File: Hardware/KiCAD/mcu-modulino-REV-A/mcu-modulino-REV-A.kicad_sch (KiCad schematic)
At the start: 9 parts, among them SW1 SW_Push, SW2 SW_Push, U8 ESP32-WROVER-E

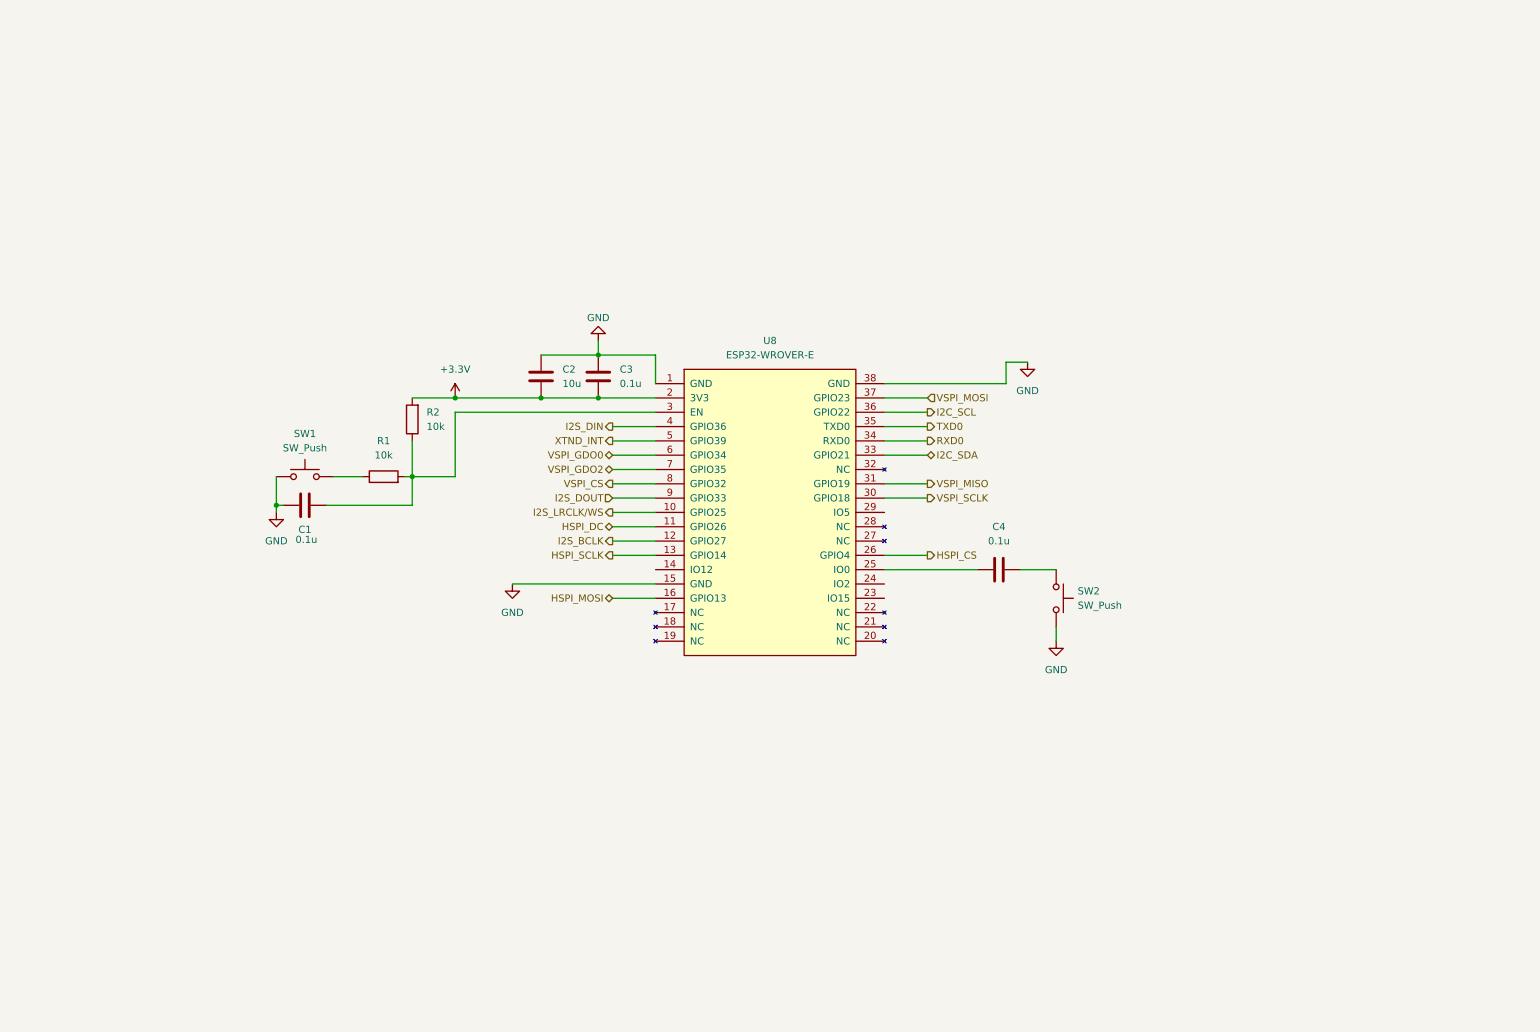
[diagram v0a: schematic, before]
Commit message: docs: update all system schematics for project uniformity
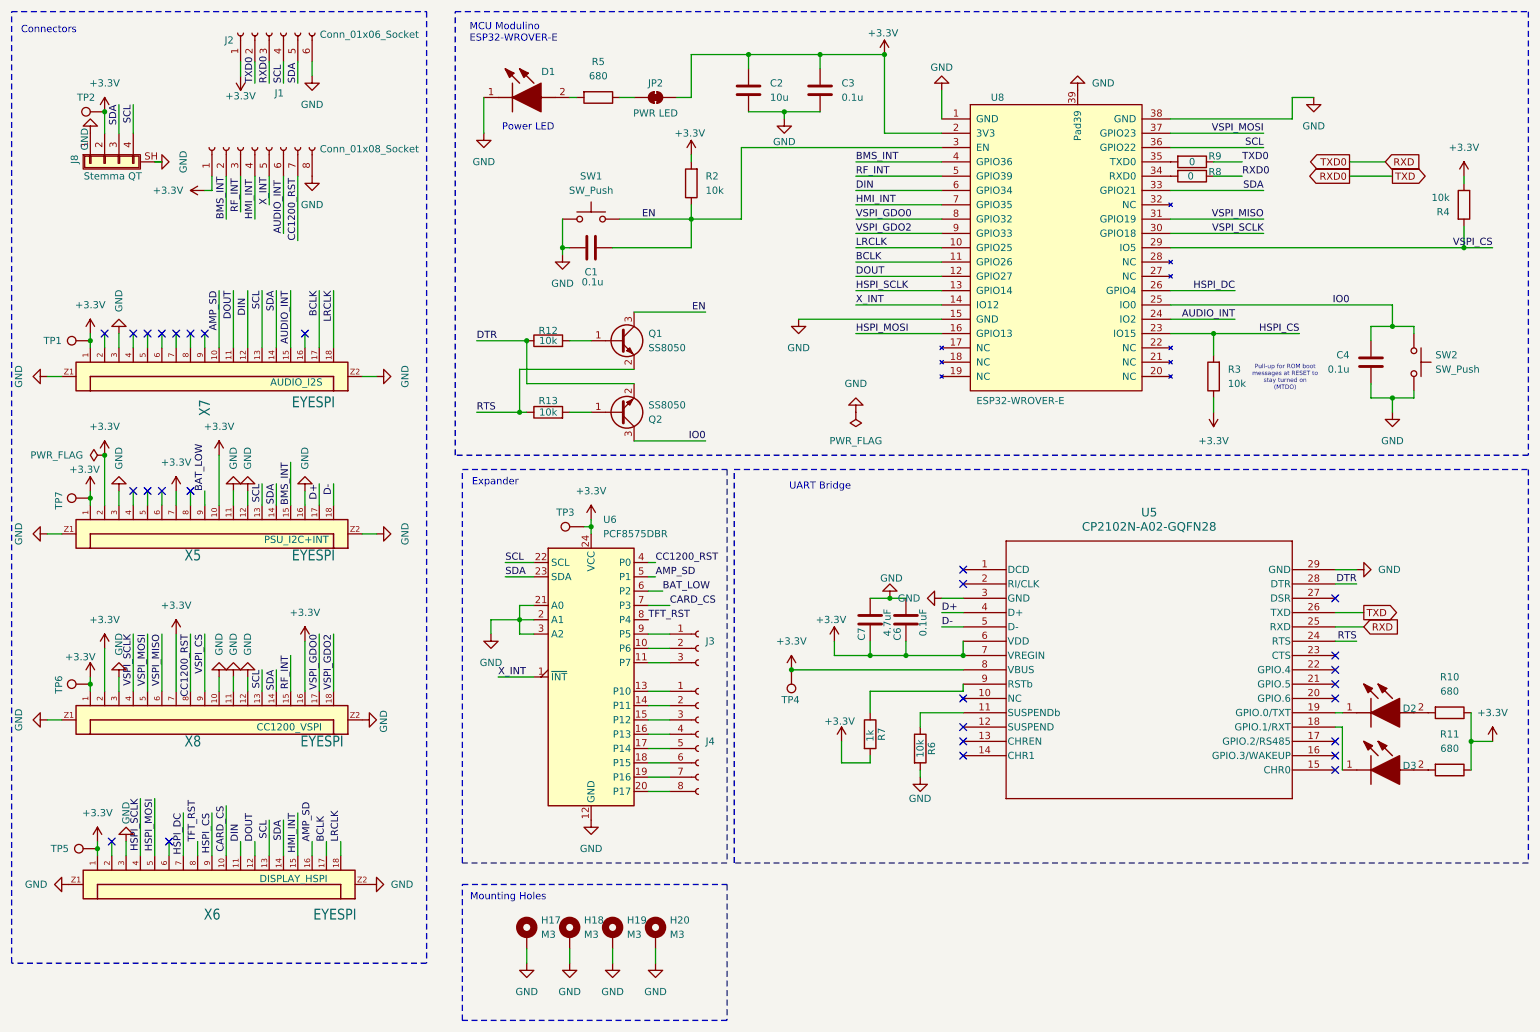
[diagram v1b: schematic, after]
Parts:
- removed R1: 10k, Resistor_SMD:R_0603_1608Metric, symbol Device:R
- added C6: 0.1uF, Capacitor_SMD:C_0603_1608Metric, symbol Device:C
- added C7: 4.7uF, Capacitor_SMD:C_0603_1608Metric, symbol Device:C
- added D1: LTST-C190KRKT, LED_SMD:LED_0603_1608Metric, symbol capstone-project:LTST-C190KRKT
- added D2, D3: LTST-C191GKT, capstone-project:LTST-C191GKT, symbol capstone-project:LTST-C191GKT
- added H17, H18, H19, H20: M3, MountingHole:MountingHole_3.2mm_M3_ISO14580_Pad, symbol Mechanical:MountingHole_Pad
- added J1: Conn_01x08_Socket, Connector_PinSocket_2.54mm:PinSocket_1x08_P2.54mm_Vertical, symbol Connector:Conn_01x08_Socket
- added J2: Conn_01x06_Socket, Connector_PinHeader_1.00mm:PinHeader_1x06_P1.00mm_Vertical, symbol Connector:Conn_01x06_Socket
- added J3: Conn_01x03_Socket, Connector_PinSocket_1.27mm:PinSocket_1x03_P1.27mm_Vertical, symbol Connector:Conn_01x03_Socket
- added J4: Conn_01x08_Socket, Connector_PinSocket_1.27mm:PinSocket_1x08_P1.27mm_Vertical, symbol Connector:Conn_01x08_Socket
- added J8: Stemma QT, Connector_JST:JST_SH_SM04B-SRSS-TB_1x04-1MP_P1.00mm_Horizontal, symbol Connector_Generic_Shielded:Conn_01x04_Shielded
- added JP2: PWR LED, Jumper:SolderJumper-2_P1.3mm_Bridged_RoundedPad1.0x1.5mm, symbol Jumper:SolderJumper_2_Bridged
- added Q1, Q2: SS8050, Package_TO_SOT_SMD:SOT-23, symbol Transistor_BJT:SS8050
- added R10, R11, R5: 680, Resistor_SMD:R_0603_1608Metric, symbol Device:R
- added R12, R13, R3, R4, R6: 10k, Resistor_SMD:R_0603_1608Metric, symbol Device:R
- added R7: 1k, Resistor_SMD:R_0603_1608Metric, symbol Device:R
- added R8, R9: 0, Resistor_SMD:R_0603_1608Metric, symbol Device:R
- added TP1, TP2, TP3, TP4, TP5, TP6, TP7: TestPoint, TestPoint:TestPoint_Pad_D1.0mm, symbol Connector:TestPoint
- added U5: CP2102N-A02-GQFN28, QFN28_5X5_SIL, symbol z:CP2102N-A02-GQFN28
- added U6: PCF8575DBR, Package_SO:SSOP-24_5.3x8.2mm_P0.65mm, symbol Interface_Expansion:PCF8575DBR
- added X5, X6, X7, X8: EYESPI, capstone-project:Adafruit EYESPI FPC Connector, symbol capstone-project:Adafruit EYESPI FPC Connector
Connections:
- net I2S_DOUT is gone; now on net VSPI_GDO2: U8.9 (GPIO33)
- net +3.3V: now also C2.1, C3.1, C6.2, C7.2, J1.1 (Pin_1), J2.1 (Pin_1), J8.2 (Pin_2), JP2.2 (B), R10.1, R11.1, R3.1, R4.1, R7.2, TP1.1, TP2.1, TP3.1, TP4.1, TP5.1, TP6.1, TP7.1, U5.6 (VDD), U5.7 (VREGIN), U5.8 (VBUS), U6.24 (VCC), X5.1, X5.10, X5.2, X5.7, X6.1, X7.1, X8.1, X8.16, X8.2, X8.7; no longer C2.2, C3.2
- net GND: now also C2.2, C3.2, C4.2, U8.39 (Pad39), C6.1, C7.1, D1.1 (K), H17.1, H18.1, H19.1, H20.1, J1.8 (Pin_8), J2.6 (Pin_6), J8.1 (Pin_1), J8.SH (Shield), R6.2, U5.29 (GND), U5.3 (GND), U6.12 (GND), U6.2 (A1), U6.21 (A0), U6.3 (A2), X5.11, X5.12, X5.16, X5.3, X5.Z1, X5.Z2, X6.3, X6.Z1, X6.Z2, X7.3, X7.Z1, X7.Z2, X8.10, X8.11, X8.12, X8.3, X8.Z1, X8.Z2; no longer C2.1, C3.1
- net HSPI_CS: now also U8.23 (IO15), R3.2, X6.9; no longer U8.26 (GPIO4)
- net HSPI_DC: now also U8.26 (GPIO4), X6.7; no longer U8.11 (GPIO26)
- net HSPI_MOSI: now also X6.5
- net HSPI_SCLK: now also X6.4
- net RXD0: now also J2.3 (Pin_3), R8.1, U5.26 (TXD); no longer U8.34 (RXD0)
- net VSPI_CS: now also U8.29 (IO5), R4.2, X8.9; no longer U8.8 (GPIO32)
- net VSPI_GDO0: now also U8.8 (GPIO32), X8.17; no longer U8.6 (GPIO34)
- net VSPI_GDO2: now also X8.18; no longer U8.7 (GPIO35)
- net VSPI_MISO: now also X8.6
- net VSPI_MOSI: now also X8.5
- net VSPI_SCLK: now also X8.4
- net EN: now reaches SW1.2
- net EN: now also C1.2, R2.1, U8.3 (EN), Q1.3 (C)
- net X_INT: now reaches U8.14 (IO12)
- net X_INT: now also J1.5 (Pin_5), U6.1 (~{INT})
- net AUDIO_INT: now reaches U8.24 (IO2)
- net AUDIO_INT: now also J1.6 (Pin_6), X7.15
- net IO0: now reaches C4.1, U8.25 (IO0)
- net IO0: now also SW2.1, Q2.3 (C)
- net I2C_SCL renamed SCL
- net SCL: now also J2.4 (Pin_4), J8.4 (Pin_4), U6.22 (SCL), X5.13, X6.13, X7.13, X8.13
- net I2C_SDA renamed SDA
- net SDA: now also J2.5 (Pin_5), J8.3 (Pin_3), U6.23 (SDA), X5.14, X6.14, X7.14, X8.14
- net I2S_BCLK renamed DOUT
- net DOUT: now also X6.12, X7.11
- net I2S_DIN renamed BMS_INT
- net BMS_INT: now also J1.2 (Pin_2), X5.15
- net I2S_LRCLK/WS renamed LRCLK
- net LRCLK: now also X6.18, X7.18
- net TXD0: no longer names the net of U8.35 (TXD0)
- net TXD0: now also R9.2
- net XTND_INT renamed RF_INT
- net RF_INT: now also J1.3 (Pin_3), X8.15
- new net: R6.1, U5.11 (SUSPENDb)
- new net: J3.2 (Pin_2), U6.10 (P6)
- new net: J3.3 (Pin_3), U6.11 (P7)
- new net: J4.1 (Pin_1), U6.13 (P10)
- new net: J4.2 (Pin_2), U6.14 (P11)
- new net: J4.3 (Pin_3), U6.15 (P12)
- new net: J4.4 (Pin_4), U6.16 (P13)
- new net: J4.5 (Pin_5), U6.17 (P14)
- new net: J4.6 (Pin_6), U6.18 (P15)
- new net: J4.7 (Pin_7), U6.19 (P16)
- new net: J4.8 (Pin_8), U6.20 (P17)
- new net: J3.1 (Pin_1), U6.9 (P5)
- new net: D3.2 (A), R11.2
- new net: D3.1 (K), U5.18 (GPIO.1/RXT)
- new net: D1.2 (A), R5.2
- new net: Q1.1 (B), R12.2
- new net: JP2.1 (A), R5.1
- new net: Q2.1 (B), R13.2
- new net: D2.1 (K), U5.19 (GPIO.0/TXT)
- new net: R7.1, U5.9 (RSTb)
- new net: D2.2 (A), R10.2
- new net: R8.2, U8.34 (RXD0)
- new net AMP_SD: U6.5 (P1), X6.16, X7.10
- new net BAT_LOW: U6.6 (P2), X5.9
- new net BCLK: U8.11 (GPIO26), X6.17, X7.17
- new net CARD_CS: U6.7 (P3), X6.10
- new net CC1200_RST: J1.7 (Pin_7), U6.4 (P0), X8.8
- new net D+: U5.4 (D+), X5.17
- new net D-: U5.5 (D-), X5.18
- new net DIN: U8.6 (GPIO34), X6.11, X7.12
- new net DTR: Q2.2 (E), R12.1, U5.28 (DTR)
- new net HMI_INT: J1.4 (Pin_4), U8.7 (GPIO35), X6.15
- new net RTS: Q1.2 (E), R13.1, U5.24 (RTS)
- new net RXD: J2.2 (Pin_2), R9.1, U5.25 (RXD)
- new net TFT_RST: U6.8 (P4), X6.8
- no-connect marks 0 -> 28
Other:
- note added: "Connectors"
- note added: "Expander"
- note added: "MCU Modulino ESP32-WROVER-E"
- note added: "Mounting Holes"
- note added: "Power LED"
- note added: "Pull-up for ROM boot messages at RESET to stay turned on (MTDO)"
- note added: "UART Bridge"
- moved on the sheet: C2, C3
